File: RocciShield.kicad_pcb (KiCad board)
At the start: 2 copper layers, 186 parts, among them J1 Battery, J10 M3, J11 I2C6, J12 Power, J13 M4, J14 I2C7, J2 I2C0, J3 I2C1, J4 I2C2, J5 I2C3, J6 M1, J7 I2C4, J8 M2, J9 I2C5, Q1 IRF7404, Q2 2N7002, U1 LMR33630, U2 LM317_TO-252, U3 LM317_TO-252, U4 TPS3700, U5 TCA9548A, U6 DRV8871, U7 DRV8871, U8 DRV8871, U9 DRV8871

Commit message: first placment finished. Needs some adjustment
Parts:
- removed D3: CDBA340-HF, Diode_SMD:D_SMA
- added C21: 100n, Capacitor_SMD:C_0603_1608Metric, F.Cu at (177.8, 100.6)
- added D32: SB10100L, Package_TO_SOT_SMD:TO-277A, F.Cu at (160.8, 86.9)
- added R65: 1k, Resistor_SMD:R_0603_1608Metric, F.Cu at (156.9, 105.8)
- C1: footprint Package_TO_SOT_SMD:SOT-23 -> Capacitor_SMD:CP_Elec_6.3x7.7
- D1, D10, D11, D12, D15, D16, D2, D20, D21, D24, D25, D30, D31, D4, D5, D9: value BAT42 -> 1N5819WS; footprint Diode_SMD:D_SOD-123 -> Diode_SMD:D_SOD-323
- F2: footprint Fuse:Fuse_0805_2012Metric -> Fuse:Fuseholder_Cylinder-5x20mm_Wuerth_696103101002-SMD_Horizontal_Open
- J1: footprint Connector_AMASS:AMASS_XT30U-M_1x02_P5.0mm_Vertical -> Connector_Phoenix_MSTB:PhoenixContact_MSTBVA_2,5_2-G_1x02_P5.00mm_Vertical
- J10: value M3 -> M2
- J13: value M4 -> M3
- J6: value M1 -> M0
- J8: value M2 -> M1
- moved JP5 195.6 mm to (203.5, 94.0), turned to -90 degrees
- moved R9 193.4 mm to (207.5, 87.1)
- moved R8 193.4 mm to (203.0, 87.1)
- moved TP8 193.4 mm to (201.1, 90.3)
- moved TP9 193.4 mm to (201.1, 91.6)
- moved C6 193.1 mm to (210.6, 87.4)
- moved JP6 192.7 mm to (206.2, 93.9), turned to -90 degrees
- moved JP7 190.2 mm to (208.8, 93.9), turned to -90 degrees
- moved U5 183.2 mm to (206.7, 93.7), turned to 90 degrees
- moved D26 177.2 mm to (186.6, 86.6)
- moved R1 173.8 mm to (209.8, 99.9), turned to 90 degrees
- moved D27 172.1 mm to (185.2, 83.6)
- moved JP1 171.3 mm to (207.5, 101.1), turned to 0 degrees
- moved R10 169.5 mm to (208.8, 106.8), turned to 90 degrees
- moved R2 168.5 mm to (207.3, 100.4), turned to 90 degrees
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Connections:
- net /M1_1 renamed /PM0_1
- net /M1_2 renamed /PM0_2
- net /M2_1 renamed /PM1_1
- net /M2_2 renamed /PM1_2
- net /M3_1 renamed /PM2_1
- net /M3_2 renamed /PM2_2
- net /M4_1 renamed /PM3_1
- net /M4_2 renamed /PM3_2
- C4 pad 2: /FB -> GND
- C5 pad 2: /FB -> GND
- Q1 pad 1: +12VA -> +12V
- Q1 pad 2: +12VA -> +12V
- Q1 pad 3: +12VA -> +12V
- Q1 pad 5: +12V -> +12VA
- Q1 pad 6: +12V -> +12VA
- Q1 pad 7: +12V -> +12VA
- Q1 pad 8: +12V -> +12VA
- TP13 pad 1: Net-(Q1-G) -> Net-(U4-OUTB)
- TP15 pad 1: M1_IN1 -> M0_IN1
- TP16 pad 1: M1_IN2 -> M0_IN2
- TP17 pad 1: M2_IN1 -> M1_IN1
- TP18 pad 1: M2_IN2 -> M1_IN2
- TP19 pad 1: M3_IN1 -> M2_IN1
- TP20 pad 1: M3_IN2 -> M2_IN2
- TP21 pad 1: M4_IN1 -> M3_IN1
- TP22 pad 1: M4_IN2 -> M3_IN2
- U4 pad 6: Net-(Q1-G) -> Net-(U4-OUTB)
- U6 pad 2: M1_IN2 -> M0_IN2
- U6 pad 3: M1_IN1 -> M0_IN1
- U7 pad 2: M2_IN2 -> M1_IN2
- U7 pad 3: M2_IN1 -> M1_IN1
- U8 pad 2: M3_IN2 -> M2_IN2
- U8 pad 3: M3_IN1 -> M2_IN1
- U9 pad 2: M4_IN2 -> M3_IN2
- U9 pad 3: M4_IN1 -> M3_IN1
- XA1 pad D11: M4_IN2 -> M2_IN2
- XA1 pad D12: M4_IN1 -> M2_IN1
- XA1 pad D5: M1_IN2 -> M0_IN2
- XA1 pad D6: M1_IN1 -> M0_IN1
- XA1 pad D7: M2_IN2 -> M1_IN2
- XA1 pad D8: M2_IN1 -> M1_IN1
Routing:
- net +5V: track 0.00 -> 104.7 mm, vias 0 -> 6
- net +12V: track 0.00 -> 99.0 mm, vias 0 -> 5
- net M0_IN2: track 0.00 -> 54.5 mm
- net M0_IN1: track 0.00 -> 50.7 mm
- net ERROR_LED: track 0.00 -> 43.3 mm
- net M1_IN2: track 0.00 -> 41.9 mm
- net M3_IN2: track 0.00 -> 41.9 mm
- net M3_IN1: track 0.00 -> 38.3 mm
- net M1_IN1: track 0.00 -> 36.8 mm
- net M2_IN2: track 0.00 -> 29.7 mm
- net M2_IN1: track 0.00 -> 26.1 mm
- net +3V3: track 0.00 -> 19.1 mm
- net Net-(U1-VCC): track 0.00 -> 14.4 mm, vias 0 -> 2
- net GND: track 0.00 -> 14.3 mm, vias 0 -> 36
- net /12V_input: track 0.00 -> 12.5 mm
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- added copper zone on B.Cu, net GND
- added copper zone on F.Cu, net GND
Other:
- board outline added: 99.6 x 53.8 mm
- board text added: "100n"

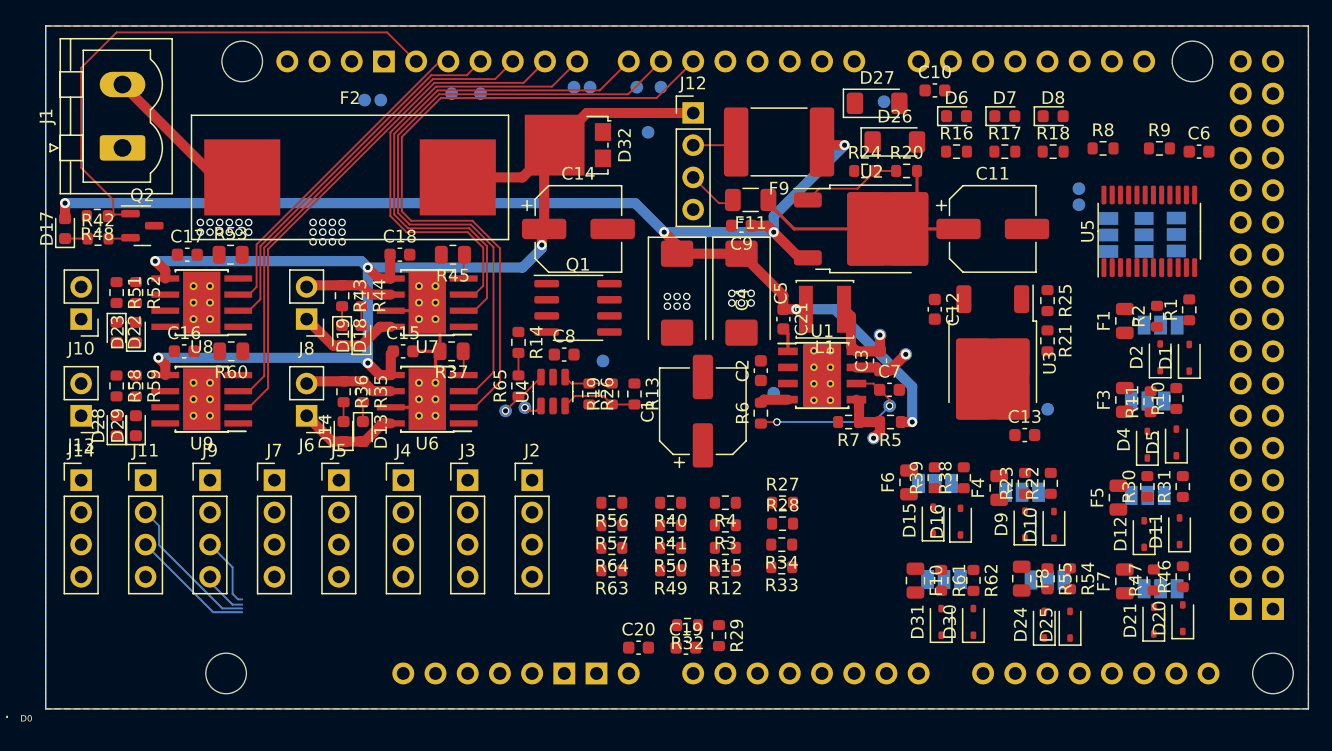
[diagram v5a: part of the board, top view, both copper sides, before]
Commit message: first finished routing. Needs some cleanup
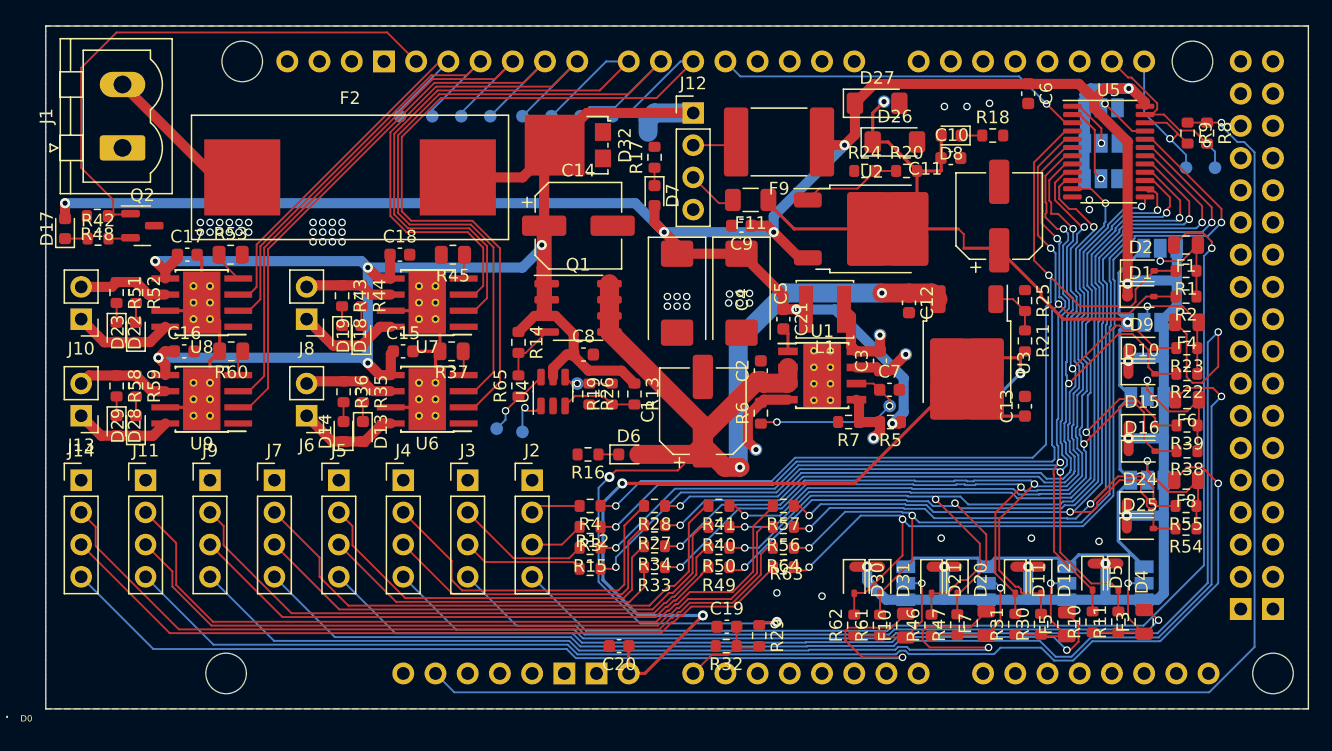
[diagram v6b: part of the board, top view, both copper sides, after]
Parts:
- moved R16 37.6 mm to (162.4, 111.3), turned to 180 degrees
- moved D6 37.1 mm to (165.6, 111.3)
- moved D7 28.3 mm to (167.6, 90.8), turned to -90 degrees
- moved R17 27.6 mm to (167.6, 87.8), turned to 90 degrees
- moved F6 22.9 mm to (209.6, 106.9), turned to 180 degrees
- moved R39 20.3 mm to (209.6, 109.0), turned to 180 degrees
- moved R46 20.2 mm to (189.5, 124.7)
- moved F4 19.7 mm to (209.6, 100.8), turned to 180 degrees
- moved R10 18.8 mm to (202.2, 124.5)
- moved D15 18.1 mm to (206.1, 109.0), turned to 0 degrees
- moved JP8 18.1 mm to (206.5, 106.7)
- moved D20 18.0 mm to (191.5, 121.2), turned to -90 degrees
- moved D21 17.8 mm to (189.5, 121.2), turned to -90 degrees
- moved R38 17.7 mm to (209.6, 111.0), turned to 180 degrees
- moved F3 17.6 mm to (206.2, 124.5)
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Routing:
- net +5V: track 104.7 -> 250.9 mm, vias 6 -> 15
- net IOREF: track 0.00 -> 112.1 mm, vias 0 -> 1
- net Net-(J11-Pin_4): track 0.00 -> 102.8 mm, vias 0 -> 1
- net Net-(J7-Pin_4): track 0.00 -> 98.7 mm, vias 0 -> 1
- net Net-(J4-Pin_4): track 0.00 -> 98.0 mm, vias 0 -> 1
- net +12VA: track 0.00 -> 97.0 mm, vias 0 -> 4
- net Net-(J2-Pin_4): track 0.00 -> 86.3 mm, vias 0 -> 1
- net Net-(D4-A): track 0.00 -> 82.2 mm, vias 0 -> 3
- net Net-(D5-A): track 0.00 -> 79.9 mm, vias 0 -> 3
- net +3V3: track 19.1 -> 98.6 mm, vias 0 -> 2
- net Net-(J14-Pin_4): track 0.00 -> 78.6 mm, vias 0 -> 1
- net Net-(D2-A): track 0.00 -> 76.9 mm, vias 0 -> 2
- net Net-(D30-A): track 0.00 -> 76.2 mm, vias 0 -> 3
- net Net-(D12-A): track 0.00 -> 76.1 mm, vias 0 -> 3
- net Net-(D1-A): track 0.00 -> 75.7 mm, vias 0 -> 3
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
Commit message: finsihed routing again
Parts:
- moved C13 52.7 mm to (144.2, 104.6), turned to 0 degrees
- moved TP16 46.9 mm to (137.7, 123.2), turned to 180 degrees
- moved U3 44.8 mm to (147.6, 100.0), turned to 180 degrees
- moved TP12 44.6 mm to (148.2, 105.0), turned to 90 degrees
- moved TP15 43.3 mm to (137.7, 120.5), turned to 180 degrees
- moved F6 42.0 mm to (170.1, 121.1), turned to -90 degrees
- moved JP8 40.7 mm to (169.8, 124.3), turned to 90 degrees
- moved R21 40.1 mm to (156.7, 101.0)
- moved R25 40.1 mm to (156.7, 97.8)
- moved TP11 39.8 mm to (200.7, 120.3)
- moved R38 39.1 mm to (171.8, 121.1), turned to -90 degrees
- moved C9 39.0 mm to (210.0, 109.3), turned to 0 degrees
- moved R39 37.8 mm to (173.9, 121.1), turned to -90 degrees
- moved C4 37.7 mm to (206.5, 105.5), turned to 180 degrees
- moved TP18 37.7 mm to (137.7, 115.3), turned to 180 degrees
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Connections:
- J11 pad 1: GND -> Net-(J11-Pin_1)
- J11 pad 2: Net-(J11-Pin_2) -> GND
- J12 pad 1: +12V -> +12VA
- J14 pad 1: GND -> Net-(J14-Pin_1)
- J14 pad 2: Net-(J14-Pin_2) -> GND
- J2 pad 1: GND -> Net-(J2-Pin_1)
- J2 pad 2: Net-(J2-Pin_2) -> GND
- J3 pad 1: GND -> Net-(J3-Pin_1)
- J3 pad 2: Net-(J3-Pin_2) -> GND
- J4 pad 1: GND -> Net-(J4-Pin_1)
- J4 pad 2: Net-(J4-Pin_2) -> GND
- J5 pad 1: GND -> Net-(J5-Pin_1)
- J5 pad 2: Net-(J5-Pin_2) -> GND
- J7 pad 1: GND -> Net-(J7-Pin_1)
- J7 pad 2: Net-(J7-Pin_2) -> GND
- J9 pad 1: GND -> Net-(J9-Pin_1)
- J9 pad 2: Net-(J9-Pin_2) -> GND
- R15 pad 2: Net-(J3-Pin_2) -> Net-(J3-Pin_1)
- R28 pad 2: Net-(J4-Pin_2) -> Net-(J4-Pin_1)
- R34 pad 2: Net-(J5-Pin_2) -> Net-(J5-Pin_1)
- R4 pad 2: Net-(J2-Pin_2) -> Net-(J2-Pin_1)
- R41 pad 2: Net-(J7-Pin_2) -> Net-(J7-Pin_1)
- R50 pad 2: Net-(J9-Pin_2) -> Net-(J9-Pin_1)
- R57 pad 2: Net-(J11-Pin_2) -> Net-(J11-Pin_1)
- R64 pad 2: Net-(J14-Pin_2) -> Net-(J14-Pin_1)
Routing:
- net I2C_RESET: track 29.4 -> 112.9 mm
- net Net-(J7-Pin_4): track 98.7 -> 19.3 mm
- net Net-(J11-Pin_4): track 102.8 -> 30.9 mm
- net Net-(J14-Pin_2): track 62.9 -> 0.00 mm
- net Net-(J11-Pin_2): track 60.9 -> 0.00 mm
- net Net-(D12-A): track 76.1 -> 16.2 mm, vias 3 -> 0
- net Net-(D11-A): track 74.2 -> 14.9 mm, vias 3 -> 0
- net Net-(J4-Pin_4): track 98.0 -> 42.2 mm
- net +12VA: track 97.0 -> 151.1 mm, vias 4 -> 2
- net Net-(D16-A): track 67.4 -> 14.7 mm, vias 3 -> 0
- net Net-(D20-A): track 74.7 -> 22.0 mm, vias 3 -> 0
- net Net-(D15-A): track 67.9 -> 15.6 mm, vias 3 -> 0
- net IOREF: track 112.1 -> 60.9 mm
- net Net-(D4-A): track 82.2 -> 31.3 mm, vias 3 -> 0
- net Net-(D21-A): track 74.1 -> 24.0 mm, vias 3 -> 0
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
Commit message: finished silcreen and 3d files
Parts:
- added C22: 100n, Capacitor_SMD:C_0603_1608Metric, F.Cu at (190.3, 90.8)
- added C23: 100n, Capacitor_SMD:C_0603_1608Metric, F.Cu at (191.3, 100.6)
- added G***: LOGO, RocciShield:RocciLogo, F.Cu at (206.1, 122.0)
- added G***: LOGO, RocciShield:RocciLogo, B.Cu at (148.3, 97.2)
- added R66: 240, Resistor_SMD:R_0603_1608Metric, F.Cu at (190.7, 98.2)
- added R67: 720, Resistor_SMD:R_0603_1608Metric, F.Cu at (190.7, 95.0)
- added U10: LM317_TO-252, Package_TO_SOT_SMD:TO-252-2, B.Cu at (193.2, 96.0)
- J10: value M2 -> M3
- J13: value M3 -> M2
- JP6: value A0 -> A1
- JP7: value A0 -> A2
- XA1: footprint PCM_arduino-library:Arduino_Mega2560_Shield -> PCM_arduino-library:Arduino_Mega2560_custom_Shield
- moved D6 35.1 mm to (157.1, 101.2), turned to -90 degrees
- moved R16 32.7 mm to (157.1, 98.0), turned to 90 degrees
- moved R25 7.18 mm to (153.9, 104.4), turned to 180 degrees
- moved R21 6.94 mm to (150.7, 104.4), turned to 180 degrees
- moved C12 3.45 mm to (154.9, 97.8), turned to -90 degrees
- moved JP6 2.84 mm to (181.7, 114.0)
- moved C20 2.82 mm to (165.7, 125.6), turned to 0 degrees
- moved JP7 2.76 mm to (178.9, 114.0)
- moved C19 2.46 mm to (168.9, 125.6), turned to 0 degrees
- moved R41 1.90 mm to (168.9, 124.0)
- moved R40 1.89 mm to (165.7, 124.0)
- moved TP7 0.95 mm to (166.5, 85.2)
- moved R64 0.44 mm to (166.9, 115.8)
- moved R56 0.37 mm to (166.9, 117.4)
- moved R57 0.29 mm to (166.9, 119.0)
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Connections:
- net Net-(JP5-C) renamed /A2
- net Net-(JP6-C) renamed /A1
- net Net-(JP7-C) renamed /A0
- D22 pad 2: /PM2_2 -> /PM3_2
- D23 pad 1: /PM2_2 -> /PM3_2
- D28 pad 2: /PM3_2 -> /PM2_2
- D29 pad 1: /PM3_2 -> /PM2_2
- J10 pad 1: /PM2_2 -> /PM3_2
- J10 pad 2: /PM2_1 -> /PM3_1
- J13 pad 1: /PM3_2 -> /PM2_2
- J13 pad 2: /PM3_1 -> /PM2_1
- R51 pad 1: /PM2_1 -> /PM3_1
- R52 pad 1: /PM2_1 -> /PM3_1
- R58 pad 1: /PM3_1 -> /PM2_1
- R59 pad 1: /PM3_1 -> /PM2_1
- TP19 pad 1: M2_IN1 -> M3_IN1
- TP20 pad 1: M2_IN2 -> M3_IN2
- TP21 pad 1: M3_IN1 -> M2_IN1
- TP22 pad 1: M3_IN2 -> M2_IN2
- U8 pad 2: M2_IN2 -> M3_IN2
- U8 pad 3: M2_IN1 -> M3_IN1
- U8 pad 6: /PM2_1 -> /PM3_1
- U8 pad 8: /PM2_2 -> /PM3_2
- U9 pad 2: M3_IN2 -> M2_IN2
- U9 pad 3: M3_IN1 -> M2_IN1
- U9 pad 6: /PM3_1 -> /PM2_1
- U9 pad 8: /PM3_2 -> /PM2_2
- XA1 pad D10: M3_IN1 -> M2_IN1
- XA1 pad D11: M2_IN2 -> M3_IN2
- XA1 pad D12: M2_IN1 -> M3_IN1
- XA1 pad D9: M3_IN2 -> M2_IN2
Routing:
- net +12VA: track 151.1 -> 169.8 mm, vias 2 -> 3
- net M3_IN1: track 40.7 -> 28.2 mm
- net M2_IN1: track 28.2 -> 40.7 mm
- net M3_IN2: track 44.1 -> 32.7 mm
- net M2_IN2: track 32.7 -> 44.1 mm
- net +5V: track 253.6 -> 263.9 mm, vias 14 -> 15
- net Net-(U10-ADJ): track 0.00 -> 7.98 mm, vias 0 -> 1
- net +8V: track 68.8 -> 62.5 mm, vias 2 -> 1
- net /A0: track 4.87 -> 8.11 mm
- net Net-(U3-ADJ): track 6.49 -> 3.78 mm
- net /A1: track 6.59 -> 4.28 mm
- net Net-(J7-Pin_1): track 5.58 -> 7.78 mm
- net Net-(D16-A): track 14.7 -> 12.6 mm
- net ADC_BAT: track 31.7 -> 33.5 mm
- net Net-(D15-A): track 15.6 -> 17.0 mm
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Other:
- board text added: "+ -"
- board text added: "+12V"
- board text added: "10A"
- board text added: "12V"
- board text added: "3,3V"
- board text added: "5V"
- board text added: "8V"
- board text added: "A0"
- board text added: "A1"
- board text added: "A2"
- board text added: "Akku"
- board text added: "BAT"
- board text added: "Boot"
- board text added: "Error"
- board text added: "FB"
- board text added: "Fuse"
- board text added: "GND"
- board text added: "I2C_0"
- board text added: "I2C_1"
- board text added: "I2C_2"
- board text added: "I2C_3"
- board text added: "I2C_4"
- board text added: "I2C_5"
- board text added: "I2C_6"
- board text added: "I2C_7"
- board text added: "I2C_RESET"
- board text added: "M0"
- board text added: "M0_IN2"
- board text added: "M1"
- board text added: "M1_IN2"
- board text added: "M2"
- board text added: "M2_IN1"
- board text added: "M2_IN2"
- board text added: "M3"
- board text added: "M3_IN1"
- board text added: "M3_IN2"
- board text added: "M_SCL"
- board text added: "M_SDA"
- board text added: "PG"
- board text added: "R_VCC"
- board text added: "RocciBoard V1.0"
- board text added: "SCL"
- board text added: "SDA"
- board text added: "SW"
- board text added: "TP10"
- board text added: "TP13"
- board text added: "TP14"
- board text added: "VCC SCL GND SDA"
